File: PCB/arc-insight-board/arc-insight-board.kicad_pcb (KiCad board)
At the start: 2 copper layers, 14.1 x 69.5 mm, 39 parts, among them J1 USB_C_Receptacle, J2 Conn_01x06, J3 Conn_01x05, J4 Conn_01x02, J5 Conn_01x02, J6 FPC_24PIN, J7 Conn_01x02, J8 U.FL, M1 Electret, U1 ESP32-S3, U2 MAX98357A, U3 MAX98357A, U4 TP4054, U5 Comparator, U6 ME6211C33M5, Y1 40MHz

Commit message: Add cap-touch firmware and TOUCH routing; refresh production outputs
- Firmware: cap-touch reading on GPIO1 (touch.cpp/h), threshold 80, 900ms hold
- PCB: route /TOUCH pad to ESP32; update schematic/project files
- Regenerate gerbers (incl. /TOUCH net), drill files, positions.csv, BOM, gerbers.zip
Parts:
- added REF**: TestPoint_THTPad_2.0x2.0mm_Drill1.0mm, TestPoint:TestPoint_THTPad_2.0x2.0mm_Drill1.0mm, F.Cu at (133.5, 131.5)
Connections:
- U1 pad 6: unconnected-(U1-GPIO1-Pad6) -> /TOUCH
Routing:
- net /TOUCH: track 0.00 -> 28.3 mm, vias 0 -> 4
- net Net-(U1-GPIO18): track 35.5 -> 38.1 mm
- net GND: track 209.6 -> 207.6 mm
- net /VBAT: track 96.9 -> 95.2 mm
- net Net-(J3-Pin_4): track 29.4 -> 30.0 mm

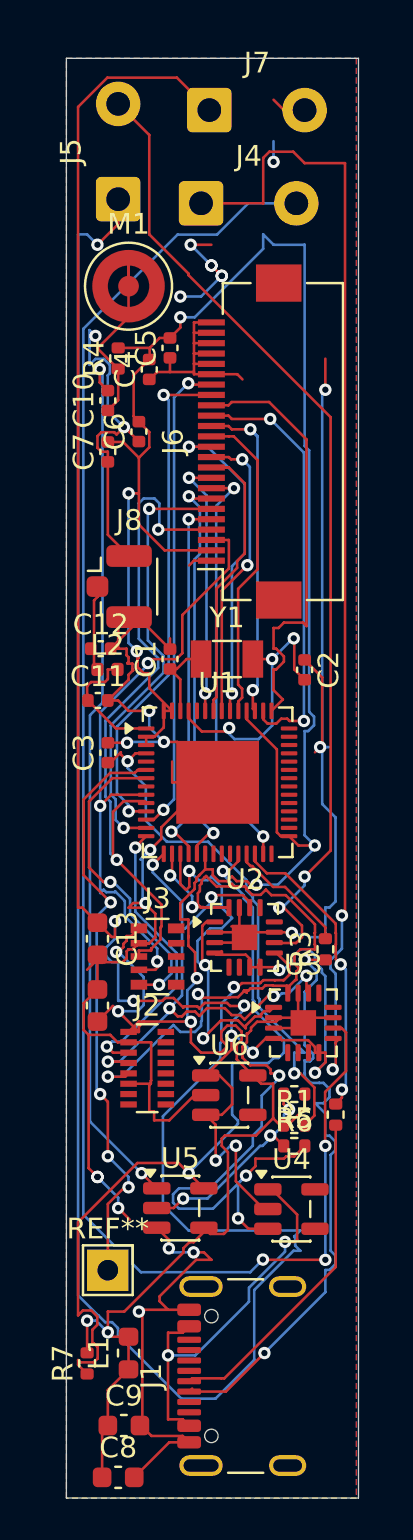
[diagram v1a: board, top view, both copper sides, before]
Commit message: Update PCB: add R8/R9 CC pulldowns, ground USB-C shield
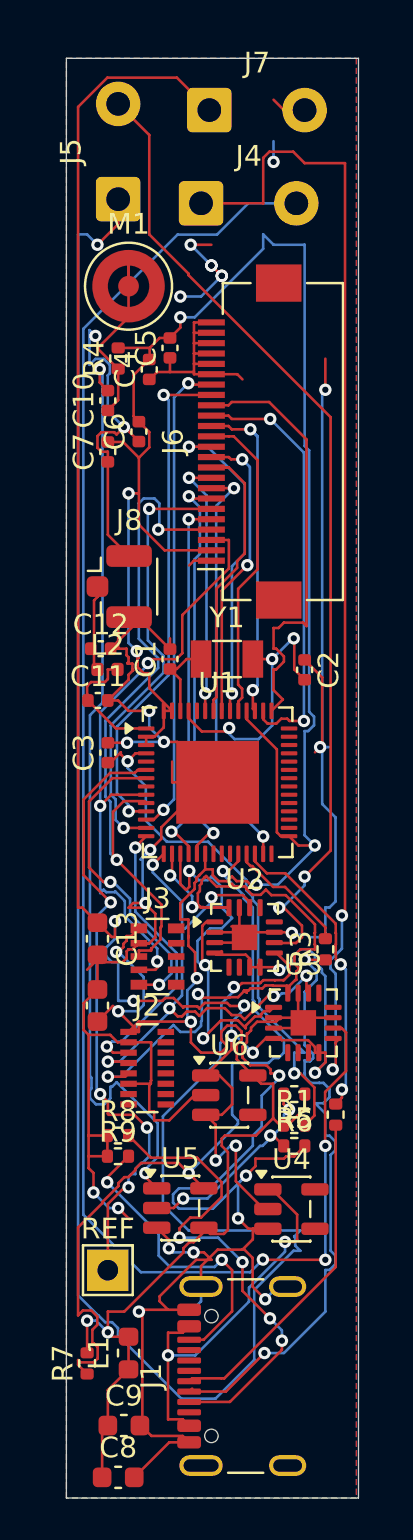
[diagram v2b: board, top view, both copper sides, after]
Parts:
- added R8: 5.1k, Resistor_SMD:R_0402_1005Metric, F.Cu at (134.0, 125.0)
- added R9: 5.1k, Resistor_SMD:R_0402_1005Metric, F.Cu at (134.0, 126.0)
- renumbered REF** to REF
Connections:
- net /ANT renamed //ANT
- net /GPIO10 renamed //GPIO10
- net /GPIO11 renamed //GPIO11
- net /GPIO12 renamed //GPIO12
- net /RF_ANT renamed //RF_ANT
- net /VBAT renamed //VBAT
- J1 pad A5: unconnected-(J1-CC1-PadA5) -> /Net-(J1-CC1-PadA5)
- J1 pad B5: unconnected-(J1-CC2-PadB5) -> /Net-(J1-CC2-PadB5)
- J1 pad SH: unconnected-(J1-SHIELD-PadSH) -> GND
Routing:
- net /Net-(J1-CC1-PadA5): track 0.00 -> 23.3 mm, vias 0 -> 4
- net /Net-(J1-CC2-PadB5): track 0.00 -> 15.0 mm, vias 0 -> 2
- net GND: track 207.6 -> 220.9 mm
- net /Net-(U5-IN+): track 42.4 -> 45.4 mm
- net /TOUCH: track 28.3 -> 30.0 mm
- net /Net-(J1-D--PadB7): track 29.3 -> 29.9 mm

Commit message: Update PCB for rewired schematic and regenerate fab outputs
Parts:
- removed L1: 1µH, Inductor_SMD:L_0603_1608Metric
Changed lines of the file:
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@@
 		)
 	)
-	(footprint "Inductor_SMD:L_0603_1608Metric"
-		(layer "F.Cu")
-		(at 134.5 135.5 90)
-		(descr "Inductor SMD 0603 (1608 Metric), square (rectangular) end terminal, IPC-7351 nominal, (Body size source: http://www.tortai-tech.com/upload/download/2011102023233369053.pdf)")
-		(tags "inductor")
-		(property "Reference" "L1"
-			(at 0 -1.43 90)
-			(layer "F.SilkS")
-			(effects
-				(font
-					(size 1 1)
-					(thickness 0.15)
-				)
-			)
-		)
-		(property "Value" "1µH"
-			(at 0 1.43 90)
-			(layer "F.Fab")
-			(effects
-				(font
-					(size 1 1)
-					(thickness 0.15)
-				)
-			)
-		)
-		(property "Datasheet" ""
-			(at 0 0 90)
-			(layer "F.Fab")
-			(hide yes)
-			(effects
-				(font
-					(size 1.27 1.27)
-				)
-			)
-		)
-		(property "Description" "Inductor"
-			(at 0 0 90)
-			(layer "F.Fab")
-			(hide yes)
-			(effects
-				(font
-					(size 1.27 1.27)
-				)
-			)
-		)
-		(property "KiLib_Generator" "SMD_2terminal_chip_molded"
-			(at 0 0 90)
-			(layer "F.SilkS")
-			(hide yes)
-			(effects
-				(font
-					(size 1 1)
-					(thickness 0.15)
-				)
-			)
-		)
-		(property "LCSC Part #" ""
-			(at 0 0 90)
-			(unlocked yes)
-			(layer "F.Fab")
-			(hide yes)
-			(effects
-				(font
-					(size 1 1)
-					(thickness 0.15)
-				)
-			)
-		)
-		(property ki_fp_filters "Choke_* *Coil* Inductor_* L_*")
-		(sheetname "/")
-		(sheetfile "arc-insight-board.kicad_sch")
-		(units
-			(unit
-				(name "A")
-				(pins "1" "2")
-			)
-		)
-		(attr smd)
-		(duplicate_pad_numbers_are_jumpers no)
-		(fp_line
-			(start -0.162779 -0.51)
-			(end 0.162779 -0.51)
-			(stroke
-				(width 0.12)
-				(type solid)
-			)
-			(layer "F.SilkS")
-		)
-		(fp_line
-			(start -0.162779 0.51)
-			(end 0.162779 0.51)
-			(stroke
-				(width 0.12)
-				(type solid)
-			)
-			(layer "F.SilkS")
-		)
-		(fp_rect
-			(start -1.48 -0.73)
-			(end 1.48 0.73)
-			(stroke
-				(width 0.05)
-				(type solid)
-			)
-			(fill no)
-			(layer "F.CrtYd")
-		)
-		(fp_rect
-			(start -0.8 -0.4)
-			(end 0.8 0.4)
-			(stroke
-				(width 0.1)
-				(type solid)
-			)
-			(fill no)
-			(layer "F.Fab")
-		)
-		(fp_text user "${REFERENCE}"
-			(at 0 0 90)
-			(layer "F.Fab")
-			(effects
-				(font
-					(size 0.4 0.4)
-					(thickness 0.06)
-				)
-			)
-		)
-		(pad "1" smd roundrect
-			(at -0.7875 0 90)
-			(size 0.875 0.95)
-			(layers "F.Cu" "F.Mask" "F.Paste")
-			(roundrect_rratio 0.25)
-			(net "VCC")
-			(pinfunction "1_1")
-			(pintype "passive")
-		)
-		(pad "2" smd roundrect
-			(at 0.7875 0 90)
-			(size 0.875 0.95)
-			(layers "F.Cu" "F.Mask" "F.Paste")
-			(roundrect_rratio 0.25)
-			(net "VCC")
-			(pinfunction "2_2")
-			(pintype "passive")
-		)
-		(embedded_fonts no)
-		(model "${KICAD10_3DMODEL_DIR}/Inductor_SMD.3dshapes/L_0603_1608Metric.step"
-			(offset
-				(xyz 0 0 0)
-			)
-			(scale
-				(xyz 1 1 1)
-			)
-			(rotate
-				(xyz 0 0 0)
-			)
-		)
-	)
 	(footprint "Connector_FFC-FPC:Hirose_FH12-24S-0.5SH_1x24-1MP_P0.50mm_Horizontal"
 		(layer "F.Cu")
@@
 		(width 0.127)
 		(layer "F.Cu")
-		(net "VCC")
-	)
-	(segment
-		(start 134.5 134.7125)
-		(end 134.6127 134.7125)
-		(width 0.127)
-		(layer "F.Cu")

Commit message: Edited files
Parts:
- turned R3 to -90 degrees
- turned R8 to 180 degrees
- turned Y1 to 180 degrees
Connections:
- net /Net-(J2-Pin_3) renamed /Net-J2Pin_3
- net /Net-(J3-Pin_3) renamed /Net-J3Pin_3
- net /Net-(J3-Pin_4) renamed /Net-J3Pin_4
- net /Net-(J3-Pin_5) renamed /Net-J3Pin_5
- net /Net-(U1-CHIP_PU) renamed /Net-CHIP_PU
- net /Net-(U1-GPIO13) renamed /Net-GPIO13
- net /Net-(U1-GPIO14) renamed /Net-GPIO14
- net /Net-(U1-GPIO18) renamed /Net-GPIO18
- net /Net-(U1-GPIO20/USB_D+) renamed /Net-GPIO20
- net /Net-(U1-GPIO21) renamed /Net-GPIO21
- net /Net-(U1-GPIO38) renamed /Net-GPIO38
- net /Net-(U1-GPIO45) renamed /Net-GPIO45
- net /Net-(U1-GPIO6) renamed /Net-GPIO6
- net /Net-(U1-GPIO7) renamed /Net-GPIO7
- net /Net-(U1-GPIO8) renamed /Net-GPIO8
- net /Net-(U1-MTCK) renamed /Net-MTCK
- net /Net-(U1-MTDI) renamed /Net-MTDI
- net /Net-(U1-MTDO) renamed /Net-MTDO
- net /Net-(U1-MTMS) renamed /Net-MTMS
- net /Net-(U1-U0RXD) renamed /Net-U0RXD
- net /Net-(U1-U0TXD) renamed /Net-U0TXD
- net /Net-(U5-IN+) renamed /Net-IN+
- net /Net-(U5-IN-) renamed /Net-IN-
- C1 pad 1: /Net-(U1-XTAL_P) -> /Net-XTAL_P
- C2 pad 2: /Net-(U1-XTAL_N) -> /Net-XTAL_N
- J1 pad A5: /Net-(J1-CC1-PadA5) -> Net-(J1-CC1)
- J1 pad B7: /Net-(J1-D--PadB7) -> Net-(J1-D--PadB7)
- R3 pad 1: /Net-(J1-D--PadB7) -> /Net-GPIO19
- R3 pad 2: /Net-(U1-GPIO19/USB_D-) -> Net-(J1-D--PadB7)
- R8 pad 1: GND -> Net-(J1-CC1)
- R8 pad 2: /Net-(J1-CC1-PadA5) -> GND
- U1 pad 25: /Net-(U1-GPIO19/USB_D-) -> /Net-GPIO19
- U1 pad 53: /Net-(U1-XTAL_N) -> /Net-XTAL_N
- U1 pad 54: /Net-(U1-XTAL_P) -> /Net-XTAL_P
- Y1 pad 1: /Net-(U1-XTAL_N) -> /Net-XTAL_P
- Y1 pad 2: /Net-(U1-XTAL_P) -> /Net-XTAL_N
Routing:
- net Net-(J1-D--PadB7): track 0.00 -> 29.9 mm, vias 0 -> 2
- net /Net-(J1-D--PadB7): track 29.9 -> 0.00 mm, vias 2 -> 0
- net Net-(J1-CC1): track 0.00 -> 23.3 mm, vias 0 -> 4
- net /Net-(J1-CC1-PadA5): track 23.3 -> 0.00 mm, vias 4 -> 0
- net /Net-XTAL_N: track 0.00 -> 13.3 mm, vias 0 -> 3
- net /Net-(U1-XTAL_N): track 13.3 -> 0.00 mm, vias 3 -> 0
- net Net-(J4-Pin_2): track 82.3 -> 93.3 mm
- net /Net-GPIO19: track 0.00 -> 6.06 mm
- net /Net-(U1-GPIO19/USB_D-): track 6.06 -> 0.00 mm
- net /Net-XTAL_P: track 0.00 -> 3.93 mm
- net /Net-(U1-XTAL_P): track 3.93 -> 0.00 mm
- net GND: track 220.9 -> 220.4 mm, vias 26 -> 23
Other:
- board text added: "ARC-Insight PCB Designed by Jadon Persun"
